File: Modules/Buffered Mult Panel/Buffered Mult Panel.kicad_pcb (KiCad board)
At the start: 2 copper layers, 48 x 175 mm, 44 parts, among them J1 TS_Jack_6.35mm_Sw, J10 TS_Jack_6.35mm_Sw, J100 IDC_02x05, J11 TS_Jack_6.35mm_Sw, J12 TS_Jack_6.35mm_Sw, J13 TS_Jack_6.35mm_Sw, J14 TS_Jack_6.35mm_Sw, J15 TS_Jack_6.35mm_Sw, J16 TS_Jack_6.35mm_Sw, J2 TS_Jack_6.35mm_Sw, J3 TS_Jack_6.35mm_Sw, J4 TS_Jack_6.35mm_Sw, J5 TS_Jack_6.35mm_Sw, J6 TS_Jack_6.35mm_Sw, J7 TS_Jack_6.35mm_Sw, J8 TS_Jack_6.35mm_Sw, J9 TS_Jack_6.35mm_Sw, U1 TL074, U2 TL074, U3 TL074

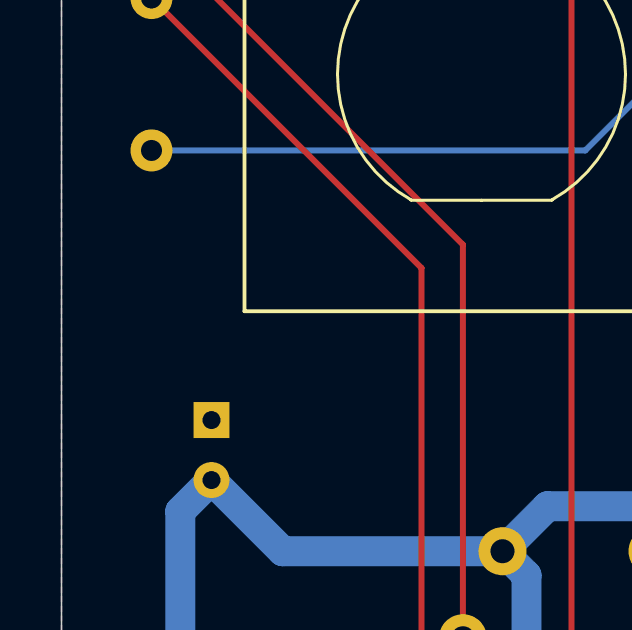
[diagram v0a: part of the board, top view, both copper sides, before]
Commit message: Added 0V solder pad and pin to panel and PCB
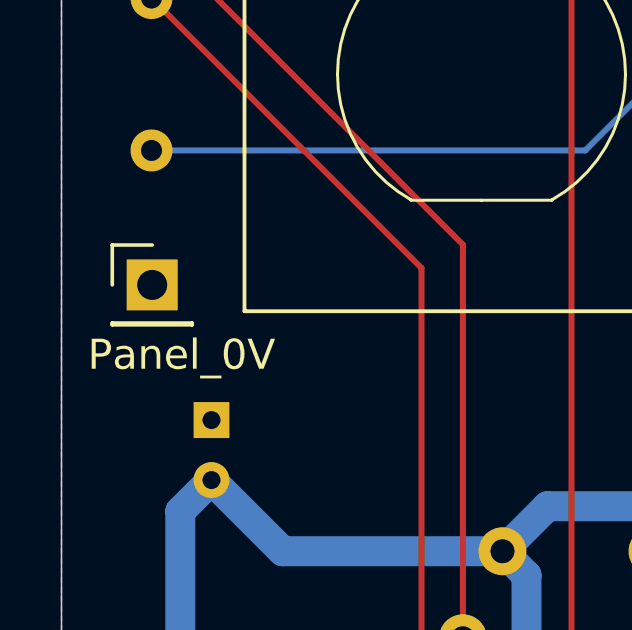
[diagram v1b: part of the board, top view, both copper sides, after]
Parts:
- added J17: Panel_0V, Connector_PinHeader_2.54mm:PinHeader_1x01_P2.54mm_Vertical, F.Cu at (29.0, 105.5)
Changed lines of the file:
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@@
+		)
+	)
+	(footprint "Connector_PinHeader_2.54mm:PinHeader_1x01_P2.54mm_Vertical"
+		(layer "F.Cu")
+		(at 29.022826 105.522826)
+		(descr "Through hole straight pin header, 1x01, 2.54mm pitch, single row")
+		(tags "Through hole pin header THT 1x01 2.54mm single row")
+		(property "Reference" "J17"
+			(at 0 -2.33 0)
+			(layer "F.SilkS")
+			(hide yes)
+			(effects
+				(font
+					(size 1 1)
+					(thickness 0.15)
+				)
+			)
+		)
+		(property "Value" "Panel_0V"
+			(at 0.977174 2.33 0)
+			(layer "F.SilkS")
+			(effects
+				(font
+					(size 1 1)
+					(thickness 0.15)
+				)
+			)
+		)
+		(property "Footprint" "Connector_PinHeader_2.54mm:PinHeader_1x01_P2.54mm_Vertical"
+			(at 0 0 0)
+			(unlocked yes)
+			(layer "F.Fab")
+			(hide yes)
+			(effects
+				(font
+					(size 1.27 1.27)
+					(thickness 0.15)
+				)
+			)
+		)
+		(property "Datasheet" ""
+			(at 0 0 0)
+			(unlocked yes)
+			(layer "F.Fab")
+			(hide yes)
+			(effects
+				(font
+					(size 1.27 1.27)
+					(thickness 0.15)
+				)
+			)
+		)
+		(property "Description" "Generic connector, single row, 01x01, script generated (kicad-library-utils/schlib/autogen/connector/)"
+			(at 0 0 0)
+			(unlocked yes)
+			(layer "F.Fab")
+			(hide yes)
+			(effects
+				(font
+					(size 1.27 1.27)
+					(thickness 0.15)
+				)
+			)
+		)
+		(property ki_fp_filters "Connector*:*_1x??_*")
+		(sheetname "Root")
+		(sheetfile "Buffered Mult Panel.kicad_sch")
+		(attr through_hole)
+		(fp_line
+			(start -1.33 -1.33)
+			(end 0 -1.33)
+			(stroke
+				(width 0.12)
+				(type solid)
+			)
+			(layer "F.SilkS")
+		)
+		(fp_line
+			(start -1.33 0)
+			(end -1.33 -1.33)
+			(stroke
+				(width 0.12)
+				(type solid)
+			)
+			(layer "F.SilkS")
+		)
+		(fp_line
+			(start -1.33 1.27)
+			(end -1.33 1.33)
+			(stroke
+				(width 0.12)
+				(type solid)
+			)
+			(layer "F.SilkS")
+		)
+		(fp_line
+			(start -1.33 1.27)
+			(end 1.33 1.27)
+			(stroke
+				(width 0.12)
+				(type solid)
+			)
+			(layer "F.SilkS")
+		)
+		(fp_line
+			(start -1.33 1.33)
+			(end 1.33 1.33)
+			(stroke
+				(width 0.12)
+				(type solid)
+			)
+			(layer "F.SilkS")
+		)
+		(fp_line
+			(start 1.33 1.27)
+			(end 1.33 1.33)
+			(stroke
+				(width 0.12)
+				(type solid)
+			)
+			(layer "F.SilkS")
+		)
+		(fp_line
+			(start -1.8 -1.8)
+			(end -1.8 1.8)
+			(stroke
+				(width 0.05)
+				(type solid)
+			)
+			(layer "F.CrtYd")
+		)
+		(fp_line
+			(start -1.8 1.8)
+			(end 1.8 1.8)
+			(stroke
+				(width 0.05)
+				(type solid)
+			)
+			(layer "F.CrtYd")
+		)
+		(fp_line
+			(start 1.8 -1.8)
+			(end -1.8 -1.8)
+			(stroke
+				(width 0.05)
+				(type solid)
+			)
+			(layer "F.CrtYd")
+		)
+		(fp_line
+			(start 1.8 1.8)
+			(end 1.8 -1.8)
+			(stroke
+				(width 0.05)
+				(type solid)
+			)
+			(layer "F.CrtYd")
+		)
+		(fp_line
+			(start -1.27 -0.635)
+			(end -0.635 -1.27)
+			(stroke
+				(width 0.1)
+				(type solid)
+			)
+			(layer "F.Fab")
+		)
+		(fp_line
+			(start -1.27 1.27)
+			(end -1.27 -0.635)
+			(stroke
+				(width 0.1)
+				(type solid)
+			)
+			(layer "F.Fab")
+		)
+		(fp_line
+			(start -0.635 -1.27)
+			(end 1.27 -1.27)
+			(stroke
+				(width 0.1)
+				(type solid)
+			)
+			(layer "F.Fab")
+		)
+		(fp_line
+			(start 1.27 -1.27)
+			(end 1.27 1.27)
+			(stroke
+				(width 0.1)
+				(type solid)
+			)
+			(layer "F.Fab")
+		)
+		(fp_line
+			(start 1.27 1.27)
+			(end -1.27 1.27)
+			(stroke
+				(width 0.1)
+				(type solid)
+			)
+			(layer "F.Fab")
+		)
+		(fp_text user "${REFERENCE}"
+			(at 0 0 90)
+			(layer "F.Fab")
+			(effects
+				(font
+					(size 1 1)
+					(thickness 0.15)
+				)
+			)
+		)
+		(pad "1" thru_hole rect
+			(at 0 0)
+			(size 1.7 1.7)
+			(drill 1)
+			(layers "*.Cu" "*.Mask")
+			(remove_unused_layers no)
+			(net 2 "GND")
+			(pinfunction "Pin_1")
+			(pintype "passive")
+		)
+		(model "${KICAD8_3DMODEL_DIR}/Connector_PinHeader_2.54mm.3dshapes/PinHeader_1x01_P2.54mm_Vertical.wrl"
+			(offset
+				(xyz 0 0 0)
+			)
+			(scale
+				(xyz 1 1 1)
+			)
+			(rotate
+				(xyz 0 0 0)
+			)
 		)
 	)

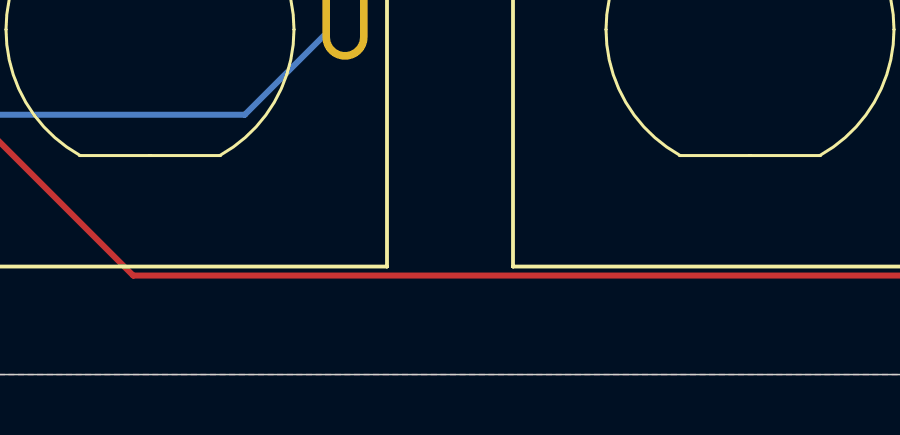
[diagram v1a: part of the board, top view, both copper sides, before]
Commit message: Updated fps to 12mm diameter
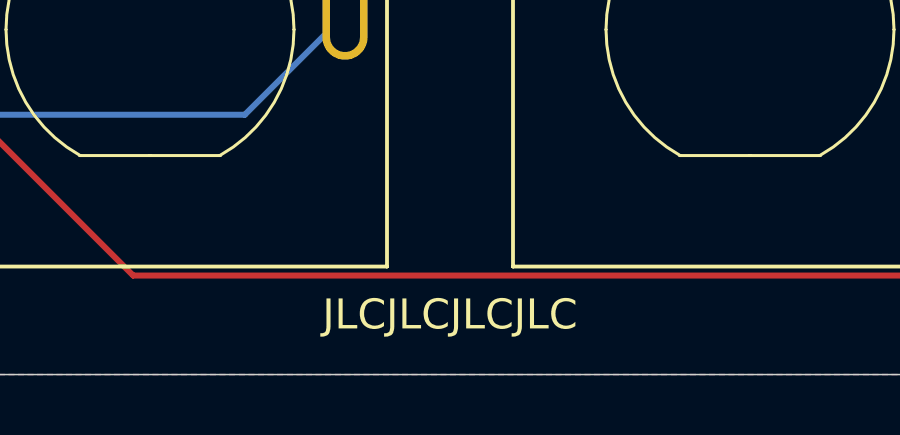
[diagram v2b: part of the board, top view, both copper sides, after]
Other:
- board text added: "Buffered Mult Mk1 - June 2024"
- board text added: "JLCJLCJLCJLC"
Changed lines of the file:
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@@
 		(layer "User.9")
+	)
+	(gr_text "Buffered Mult Mk1 - June 2024"
+		(at 50 210.5 0)
+		(layer "B.SilkS")
+		(effects
+			(font
+				(size 1 1)
+				(thickness 0.1)
+			)
+			(justify mirror)
+		)
+	)
+	(gr_text "JLCJLCJLCJLC"
+		(at 50 210.5 0)
+		(layer "F.SilkS")
+		(effects
+			(font
+				(size 1 1)
+				(thickness 0.1)
+			)
+		)
 	)
 	(segment

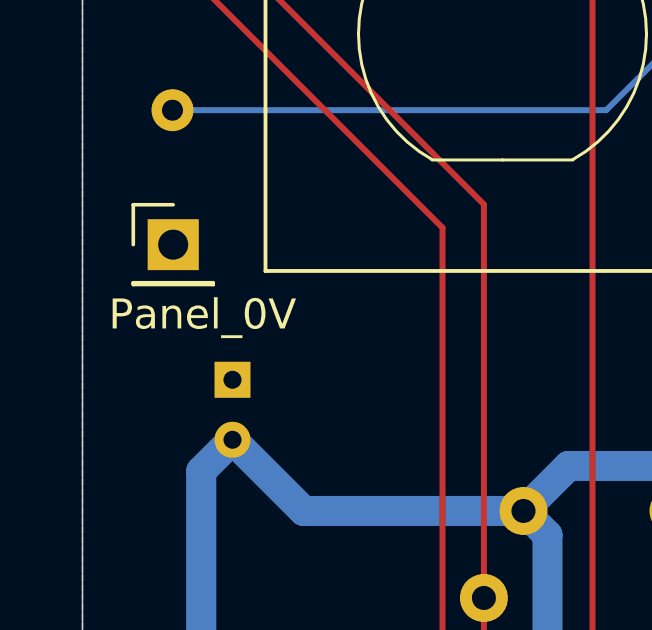
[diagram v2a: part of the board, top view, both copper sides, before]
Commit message: Changed Panel 0V to Panel GND
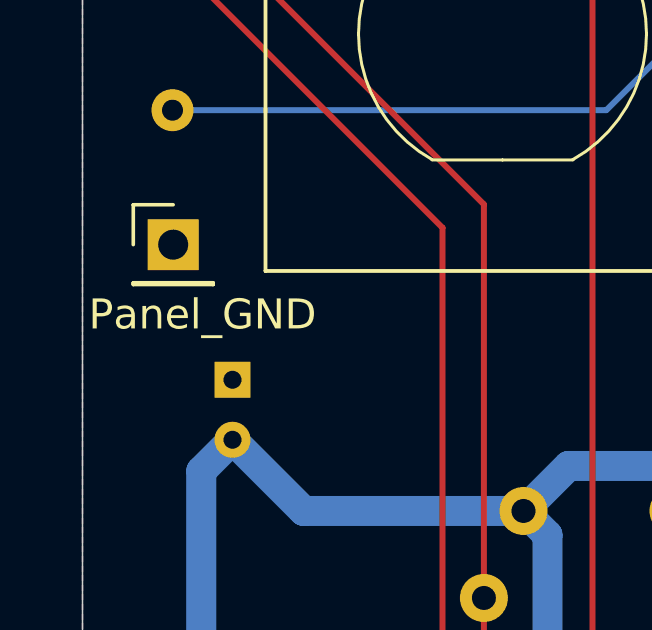
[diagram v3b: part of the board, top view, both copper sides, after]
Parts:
- J17: value Panel_0V -> Panel_GND
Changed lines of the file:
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@@
 			)
 		)
-		(property "Value" "Panel_0V"
+		(property "Value" "Panel_GND"
 			(at 0.977174 2.33 0)
 			(layer "F.SilkS")

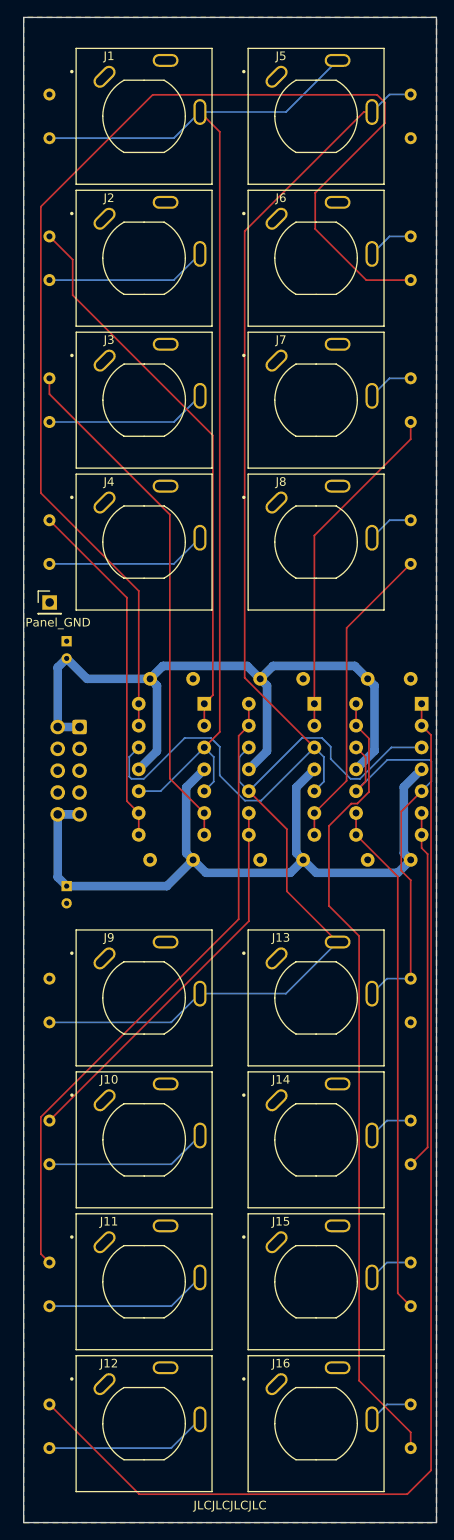
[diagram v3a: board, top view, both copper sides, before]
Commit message: Replaced resistors with 1/4 W
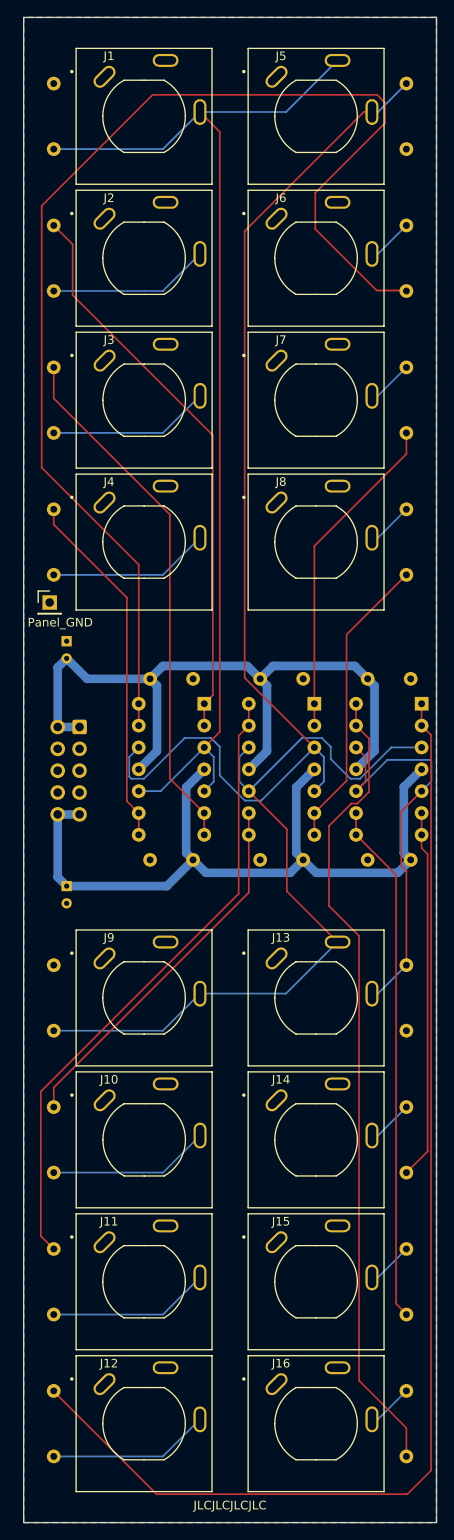
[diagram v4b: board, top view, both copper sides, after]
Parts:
- R1, R10, R11, R12, R13, R14, R15, R16, R2, R3, R4, R5, R6, R7, R8, R9: footprint Resistor_THT:R_Axial_DIN0204_L3.6mm_D1.6mm_P5.08mm_Horizontal -> Resistor_THT:R_Axial_DIN0207_L6.3mm_D2.5mm_P7.62mm_Horizontal
- moved R10 1.65 mm to (29.5, 164.2)
- moved R11 1.65 mm to (29.5, 180.7)
- moved R12 1.65 mm to (29.5, 197.2)
- moved R9 1.65 mm to (29.5, 147.7)
- moved R1 1.36 mm to (29.5, 45.2)
- moved R2 1.36 mm to (29.5, 61.7)
- moved R5 1.36 mm to (70.5, 52.8)
- moved R3 1.36 mm to (29.5, 78.2)
- moved R4 1.36 mm to (29.5, 94.7)
- moved R6 1.36 mm to (70.5, 69.3)
- moved R7 1.36 mm to (70.5, 85.8)
- moved R8 1.36 mm to (70.5, 102.3)
- moved R13 1.09 mm to (70.5, 155.3)
- moved R14 1.09 mm to (70.5, 171.8)
- moved R15 1.09 mm to (70.5, 188.3)
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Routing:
- net Net-(U2C--): track 45.4 -> 43.6 mm
- net Net-(U3B-+): track 48.7 -> 47.1 mm
- net Net-(U2B--): track 36.1 -> 34.7 mm
- net Net-(U2A--): track 39.9 -> 38.5 mm
- net Net-(U2D--): track 75.4 -> 74.0 mm
- net Net-(U3B--): track 41.9 -> 43.1 mm
- net Net-(U1B--): track 60.5 -> 61.6 mm
- net Net-(U1C--): track 40.9 -> 41.9 mm
- net Net-(U1A--): track 65.2 -> 66.2 mm
- net Net-(U3D--): track 93.4 -> 94.2 mm
- net Net-(U3C--): track 60.0 -> 60.7 mm
